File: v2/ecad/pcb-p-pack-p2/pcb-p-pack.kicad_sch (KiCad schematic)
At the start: 56 parts, among them Q1 CSD17570Q5B 30 V N-FET, charg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, Q2 CSD17570Q5B 30 V N-FET, disch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, U1 BQ4050RSMR: SMBus 1.1 gas gau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

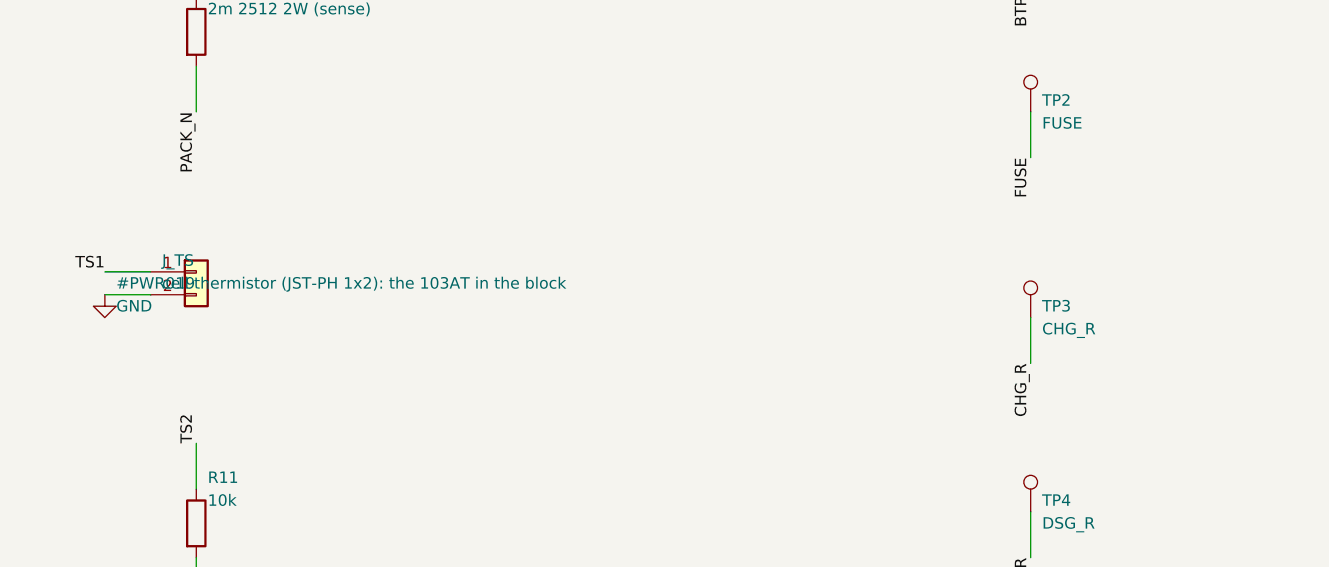
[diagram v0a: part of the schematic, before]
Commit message: feat(pcb-p): P3 is re-cut, and every part on it is orderable [MESHSAT-862]
routeflow ended CLEAN: hard 0, unrouted 0, 55 vias, board sha256 5ae0ce7e matching the deliverable's own
record.

It took four attempts and each one was refused for a different reason, every one of them real:

  1  a blank BOM code, because the thermistor row's comment reword stopped matching an lcsc-allow line
     that should never have covered a socket in the first place
  2  a locked GND via dead at its B.Cu end, and the tool written for exactly that refused to touch it
     because two tracks landed on it, both on F.Cu
  3  the same defect at a different via, because the exposed pad of the BQ4050 had one thermal via
     instead of four and the fill had retreated from it
  4  the pruner declared at the top level of boards/p.json, where finish.sh cannot see it

jlc_certify on P: 19 components, 19 CERTIFIED, nothing hand-fit, nothing bench-fitted, nothing open.
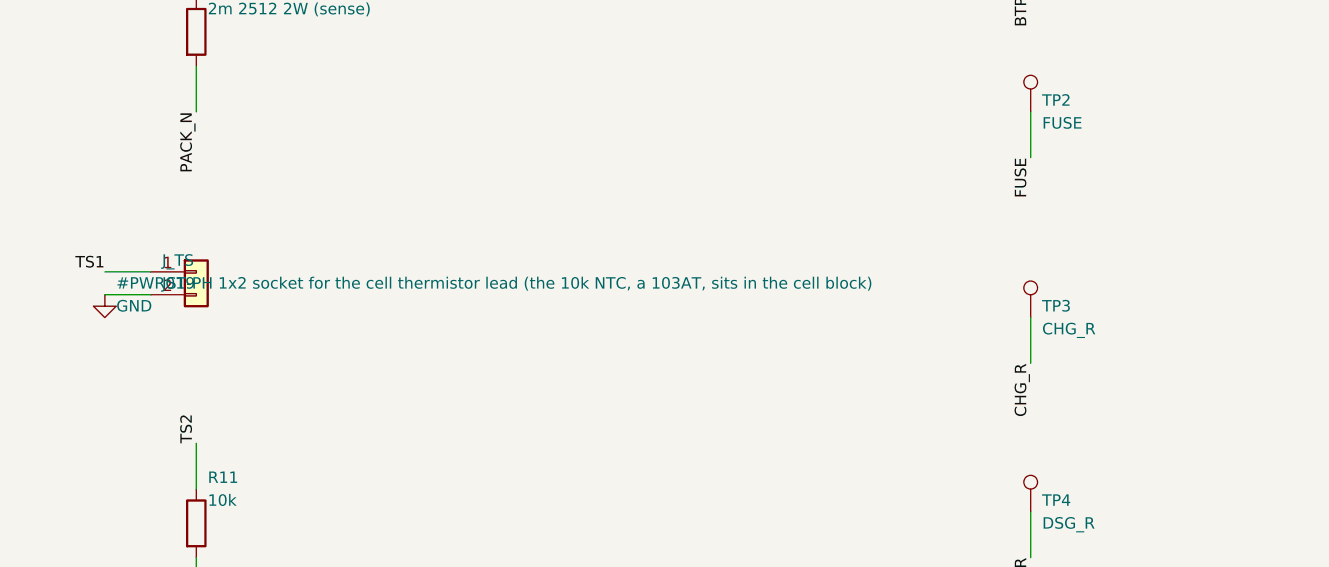
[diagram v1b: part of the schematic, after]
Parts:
- J_TS: value cell thermistor (JST-PH 1x2): the 103AT in the block -> JST-PH 1x2 socket for the cell thermistor lead (the 10k NTC, a 103AT, sits in the cell block); LCSC (none) -> C5251182
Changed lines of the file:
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@@
 	(symbol (lib_id "Connector_Generic:Conn_01x02") (at 39.37 734.06 0) (unit 1) (exclude_from_sim no) (in_bom yes) (on_board yes) (dnp no) (fields_autoplaced yes)
 		(property "Reference" "J_TS" (at 35.56 732.79 0) (effects (font (size 1.27 1.27)) (justify left)))
-		(property "Value" "cell thermistor (JST-PH 1x2): the 103AT in the block" (at 35.56 735.33 0) (effects (font (size 1.27 1.27)) (justify left)))
+		(property "Value" "JST-PH 1x2 socket for the cell thermistor lead (the 10k NTC, a 103AT, sits in the cell block)" (at 35.56 735.33 0) (effects (font (size 1.27 1.27)) (justify left)))
 		(property "Footprint" "Connector_JST:JST_PH_B2B-PH-K_1x02_P2.00mm_Vertical" (at 39.37 734.06 0) (effects (font (size 1.27 1.27)) (justify left) (hide yes)))
 		(property "Datasheet" "" (at 39.37 734.06 0) (effects (font (size 1.27 1.27)) (justify left) (hide yes)))
 		(property "Description" "" (at 39.37 734.06 0) (effects (font (size 1.27 1.27)) (justify left) (hide yes)))
+		(property "LCSC" "C5251182" (at 39.37 734.06 0) (effects (font (size 1.27 1.27)) (justify left) (hide yes)))
 		(pin "1")
 		(pin "2")

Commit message: feat(ecad): readable schematics: a page engine draws every board as wired A3 pages of functional blocks (ICs as boxes with rails top and grounds bottom, passives on the pins they serve, decoupling rows, power symbols), proves the drawing's connectivity before writing, and the build cuts the sheet into A3 pages; all six netlists identical; the render scene puts the lit display on the glass and the monitor's rear block under it [MESHSAT-862]
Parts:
- removed C2, C9: 100n, Capacitor_SMD:C_0603_1608Metric, symbol Device:C
- removed Q1: CSD17570Q5B 30 V N-FET, charge switch, Package_SO:PowerPAK_SO-8_Single, symbol Connector_Generic:Conn_01x05
- removed Q2: CSD17570Q5B 30 V N-FET, discharge switch, Package_SO:PowerPAK_SO-8_Single, symbol Connector_Generic:Conn_01x05
- removed R12, R15: 10k, Resistor_SMD:R_0603_1608Metric, symbol Device:R
- added C3: 100n, Capacitor_SMD:C_0603_1608Metric, symbol Device:C
- added Q1: CSD17570Q5B 30 V N-FET, charge switch, Package_SO:PowerPAK_SO-8_Single, symbol meshsat_ic:Q1
- added Q2: CSD17570Q5B 30 V N-FET, discharge switch, Package_SO:PowerPAK_SO-8_Single, symbol meshsat_ic:Q2
- added R4, R9: 100R, Resistor_SMD:R_0603_1608Metric, symbol Device:R
- added R7: 1k, Resistor_SMD:R_0603_1608Metric, symbol Device:R
- C2: renamed from R4; value 100R -> 100n; footprint Resistor_SMD:R_0603_1608Metric -> Capacitor_SMD:C_0603_1608Metric; symbol Device:R -> Device:C
- C9: renamed from R7; value 1k -> 100n; footprint Resistor_SMD:R_0603_1608Metric -> Capacitor_SMD:C_0603_1608Metric; symbol Device:R -> Device:C
- R12: renamed from R9; value 100R -> 10k
- R15: renamed from C3; value 100n -> 10k; footprint Capacitor_SMD:C_0603_1608Metric -> Resistor_SMD:R_0603_1608Metric; symbol Device:C -> Device:R
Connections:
- net CELL4: now also R4.1; no longer C2.1
- net CHG_G: now also Q1.4 (CHG_G)
- net DISP: now also R15.1
- net DSG_G: now also Q2.4 (DSG_G)
- net FUSED: now also Q1.1 (FUSED), Q1.2 (FUSED), Q1.3 (FUSED)
- net GND: now also C2.2, R12.2, C3.2
- net PACK_N: now also R9.1; no longer R12.1
- net PACK_P: now also Q2.1 (PACK_P), Q2.2 (PACK_P), Q2.3 (PACK_P), R7.1; no longer C9.1
- net SRN_F: now also C9.2, R9.2; no longer R12.2
- net SRP_F: now also C9.1
- net SW: now also Q1.5 (SW), Q2.5 (SW)
- net TS3: now also R12.1
- net VC1_F: now also C2.1
- net VC2_F: now also C3.1; no longer R15.1
- net VC4_F: now also R4.2; no longer C2.2
- net VCC_F: now also R7.2; no longer C9.2
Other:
- note added: "25 A mini blade"
- note added: "2m 2512 2W"
- note added: "BQ4050RSMR"
- note added: "CELL TAPS, GAUGE BQ4050, SENSE AND SUPPLY FILTERS, THERMISTOR | FUSE, PROTECTION FETS, GATE NETWORKS, TERMINAL ESD, PACK LEADS | SMBUS OUT, TEST POINTS, FLAGS"
- note added: "CSD17570Q5B 30 V N-FET"
- note added: "JST-PH 1x2 socket for the cell the.."
- note added: "PCB-P PACK BMS P4"
- note added: "SMBus lead to E6 J_SMB"
- note added: "USBLC6-2SC6 ESD clamp on the SMBus.."
- note added: "cell block B+"
- note added: "cell block B-"
- note added: "cell tap sense wires from the 4S b.."
- note added: "decoupling of U1"
- note added: "pack lead +"
- note added: "pack lead -"
- note added: "page 1 of 1 MeshSat field kit V2, CERN-OHL-S-2.0 PROTOTYPE, nothing built 2026-09-15"
- moved on the sheet: R12, R18

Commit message: feat(ecad): the schematic pages draw every net that stays on a page as wires between its parts and mark every signal that leaves a page with the pages it goes to; B's shared area is sectioned by its generator headings; six netlists identical [MESHSAT-862]
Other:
- note removed: "decoupling of U1"
- moved on the sheet: C1, C10, C2, C3, C4, C5, C6, C7, C9, R10, R11, R12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

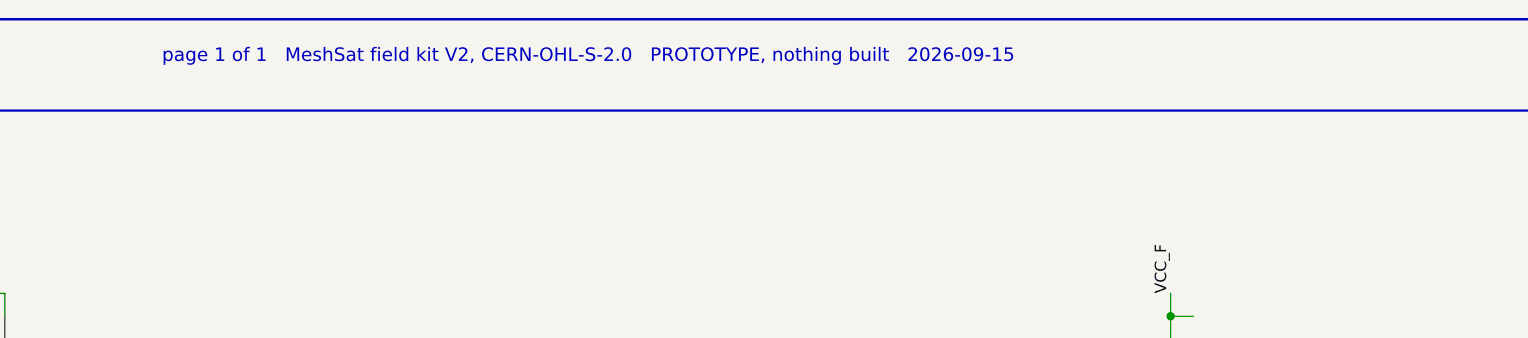
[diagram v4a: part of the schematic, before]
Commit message: fix(ecad): the six committed netlists came from schematics this tree does not hold [MESHSAT-862]
`sch_prov.py` records the sha256 of the schematic a netlist was generated from,
and on every one of the six boards it named a schematic that is not the one in
the repo: the netlists were regenerated and committed at 00:14 this morning
without their schematics, which are from 15 and 16 September. Board E is the
clearest case, its committed netlist carrying the SMCJ40A and the 100 V bulk
capacitor of the suppressor pass while its committed drawing still showed the
SMCJ33A they replaced.

Only board B tripped the timestamp guard, because only board B's schematic had
been rewritten (with identical content) after the netlist, so the contract gate
refused board B and passed five boards in the identical state. That is a guard
reading a proxy while the fact sits beside it.

- check_contracts compares the sidecar's schematic hash when there is one and
  keeps the mtime rule only for a netlist with no provenance. A rule holds both
  directions and fails on the pre-fix source ("a netlist generated from a
  schematic this tree does not hold was accepted because its mtime is older").
- the six schematics are regenerated by today's generators at each board's own
  declared phase, and each board's netlist was exported from the new schematic
  and compared with the committed one component by component and node by node:
  398/262, 931/1852, 194/144, 207/172, 161/118 and 56/39 components and nets
  agree on every node. No connectivity moved; what moved is the drawing, which
  had been left behind, and E's two part values, which the netlist already had.
  erc_gate PASS on all six.
- the contract gate on this tree now reads PASS of 72 where it read INCONCLUSIVE
  of 54 with 24 contracts unjudged, which is SCH-003 and INT-001 on six boards.

Suite 928 passing, 0 failing, 19 skipped.
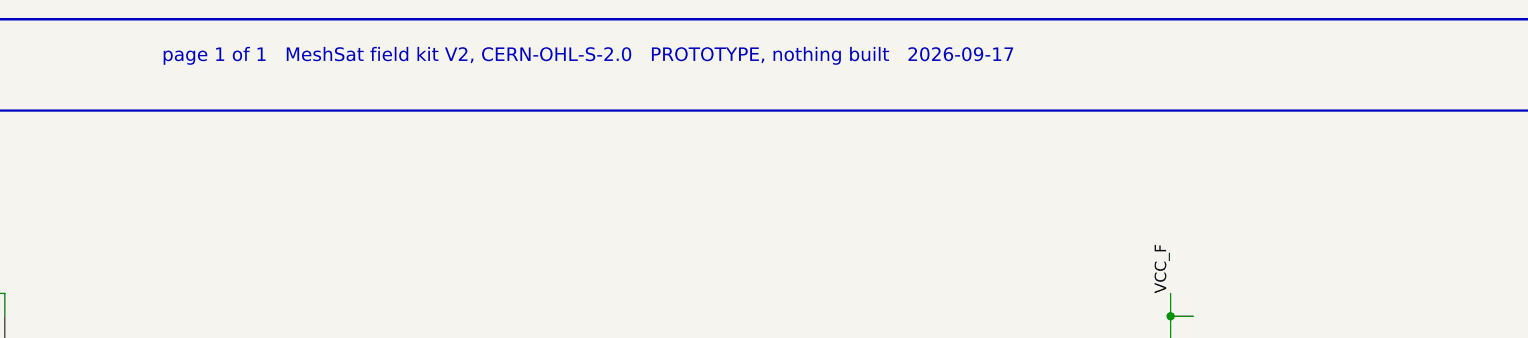
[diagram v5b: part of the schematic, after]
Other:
- note added: "page 1 of 1 MeshSat field kit V2, CERN-OHL-S-2.0 PROTOTYPE, nothing built 2026-09-17"
- note removed: "page 1 of 1 MeshSat field kit V2, CERN-OHL-S-2.0 PROTOTYPE, nothing built 2026-09-15"
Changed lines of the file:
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@@
 	(generator_version "9.0")
 	(paper "User" 419.10 297.18)
-	(title_block (title "MeshSat Field Kit carrier - PCB-P PACK BMS") (date "2026-09-15") (rev "A") (company "MeshSat") (comment 1 "Phase P4 schematic (BQ4050 SMBus gauge and protection for the built 4S pack; appendix 32.62), generated by tools/gen_sch_p.py"))
+	(title_block (title "MeshSat Field Kit carrier - PCB-P PACK BMS") (date "2026-09-17") (rev "A") (company "MeshSat") (comment 1 "Phase P4 schematic (BQ4050 SMBus gauge and protection for the built 4S pack; appendix 32.62), generated by tools/gen_sch_p.py"))
 	(rectangle (start 2.54 2.54) (end 416.56 294.64) (stroke (width 0.25) (type default)) (fill (type none)))
 	(rectangle (start 2.54 2.54) (end 416.56 12.70) (stroke (width 0.25) (type default)) (fill (type none)))
@@
 	(text "FUSE, PROTECTION FETS, GATE NETWORKS, TERMINAL ESD, PACK LEADS" (exclude_from_sim no) (at 10.16 137.16 0) (effects (font (size 1.80 1.80) bold) (justify left bottom)))
 	(text "SMBUS OUT, TEST POINTS, FLAGS" (exclude_from_sim no) (at 10.16 205.74 0) (effects (font (size 1.80 1.80) bold) (justify left bottom)))
-	(text "page 1 of 1   MeshSat field kit V2, CERN-OHL-S-2.0   PROTOTYPE, nothing built   2026-09-15" (exclude_from_sim no) (at 258.77 7.62 0) (effects (font (size 1.50 1.50)) (justify left bottom)))
+	(text "page 1 of 1   MeshSat field kit V2, CERN-OHL-S-2.0   PROTOTYPE, nothing built   2026-09-17" (exclude_from_sim no) (at 258.77 7.62 0) (effects (font (size 1.50 1.50)) (justify left bottom)))
 	(symbol (lib_id "Connector_Generic:Conn_01x05") (at 52.07 35.56 0) (unit 1) (exclude_from_sim no) (in_bom yes) (on_board yes) (dnp no)
 		(property "Reference" "J_CELL" (at 54.61 25.93 0) (effects (font (size 1.27 1.27)) (justify left bottom)))

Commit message: fix(ecad): the six netlists regenerated, and a reading that lacked its input could displace one that had it [MESHSAT-862]
Sweep 28 re-took every gate on all seven boards, read-only, and no board changed. Readiness went 62.8 to 54.1
percent, and reading that before reporting it found two things.

Eighty-four verdicts in twelve shapes said their input was absent in the NOTE and declared nothing in the
missing_input FIELD, which defeats the one mechanism that crosses hosts: rules_status prefers the reading
that HAD its input and all it can read is that field. check_contracts even carries a _richer_on_disk guard
and it cannot help, because it protects a better reading in THIS tree. check_contracts (per board, per
inhibit chain and set-level) and stackup_gate declare it now, and a DATA rule reads the tree's own verdicts
and refuses any that says its input was absent in prose while declaring nothing. Run against the sweep's
output it names all 84.

And half my first diagnosis was wrong, corrected within ten minutes. I called the netlist half a staging gap.
Asked directly rather than inferred, check_contracts prints UNKNOWN GENERATOR on the box and on the runner
identically: the generator identity is gen_sch_<L>.py plus kisch.py plus intent.py by content, and intent.py
changed four times since the netlists were last regenerated on 18 September. So SCH-003 on six boards and
INT-001 on seven have been INCONCLUSIVE on every host for two days while the page carried the 18 September
pass nobody re-took, which is board B's MEC-001 this morning in the largest cross-board gate. stackup_gate
really was a staging gap and reads PASS of 24 here.

Regen 7 rebuilt all six at their declared phases: A, C, D, E and P identical connection for connection
(2,386 / 1,067 / 1,193 / 955 / 295 lines), board B different by 804 lines every one of which is a net class,
which is the defect named on 20 September at 05:26 and this is what fixes it. The three files move as one:
with the netlists and sid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
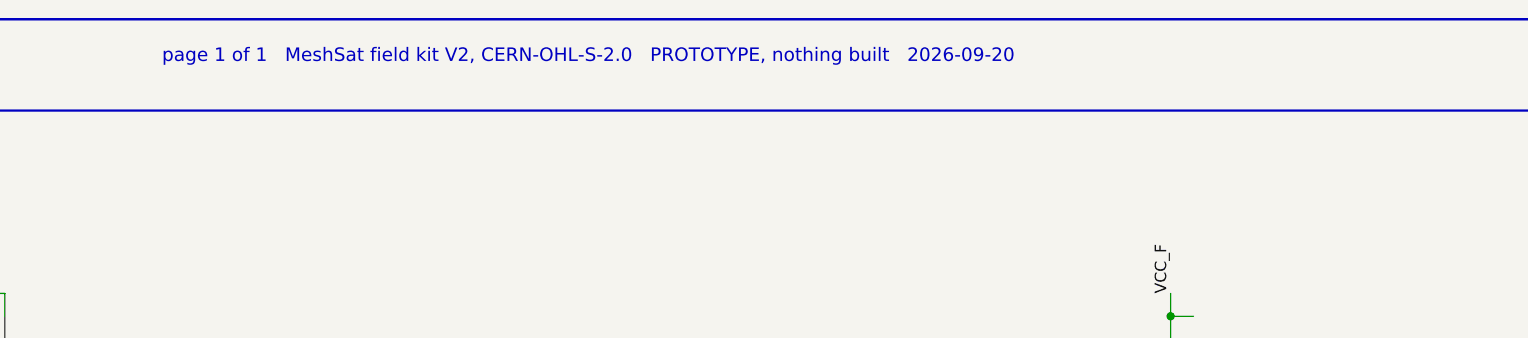
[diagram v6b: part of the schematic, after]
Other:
- note added: "page 1 of 1 MeshSat field kit V2, CERN-OHL-S-2.0 PROTOTYPE, nothing built 2026-09-20"
- note removed: "page 1 of 1 MeshSat field kit V2, CERN-OHL-S-2.0 PROTOTYPE, nothing built 2026-09-17"
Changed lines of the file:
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@@
 	(generator_version "9.0")
 	(paper "User" 419.10 297.18)
-	(title_block (title "MeshSat Field Kit carrier - PCB-P PACK BMS") (date "2026-09-17") (rev "A") (company "MeshSat") (comment 1 "Phase P4 schematic (BQ4050 SMBus gauge and protection for the built 4S pack; appendix 32.62), generated by tools/gen_sch_p.py"))
+	(title_block (title "MeshSat Field Kit carrier - PCB-P PACK BMS") (date "2026-09-20") (rev "A") (company "MeshSat") (comment 1 "Phase P4 schematic (BQ4050 SMBus gauge and protection for the built 4S pack; appendix 32.62), generated by tools/gen_sch_p.py"))
 	(rectangle (start 2.54 2.54) (end 416.56 294.64) (stroke (width 0.25) (type default)) (fill (type none)))
 	(rectangle (start 2.54 2.54) (end 416.56 12.70) (stroke (width 0.25) (type default)) (fill (type none)))
@@
 	(text "FUSE, PROTECTION FETS, GATE NETWORKS, TERMINAL ESD, PACK LEADS" (exclude_from_sim no) (at 10.16 137.16 0) (effects (font (size 1.80 1.80) bold) (justify left bottom)))
 	(text "SMBUS OUT, TEST POINTS, FLAGS" (exclude_from_sim no) (at 10.16 205.74 0) (effects (font (size 1.80 1.80) bold) (justify left bottom)))
-	(text "page 1 of 1   MeshSat field kit V2, CERN-OHL-S-2.0   PROTOTYPE, nothing built   2026-09-17" (exclude_from_sim no) (at 258.77 7.62 0) (effects (font (size 1.50 1.50)) (justify left bottom)))
+	(text "page 1 of 1   MeshSat field kit V2, CERN-OHL-S-2.0   PROTOTYPE, nothing built   2026-09-20" (exclude_from_sim no) (at 258.77 7.62 0) (effects (font (size 1.50 1.50)) (justify left bottom)))
 	(symbol (lib_id "Connector_Generic:Conn_01x05") (at 52.07 35.56 0) (unit 1) (exclude_from_sim no) (in_bom yes) (on_board yes) (dnp no)
 		(property "Reference" "J_CELL" (at 54.61 25.93 0) (effects (font (size 1.27 1.27)) (justify left bottom)))
